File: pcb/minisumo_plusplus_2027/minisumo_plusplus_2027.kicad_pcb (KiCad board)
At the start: 2 copper layers, 45 x 33 mm, 11 parts, among them J1 IR - Conn_01x03_Pin, J2 IR - Conn_01x03_Pin, J3 Start Module - Conn_01x04_Pin, J4 US - Conn_01x04_Pin, SW1 SW_SPDT, U3 ESP32-C6-SuperMini

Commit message: pcb updates to clean up a abit, drc was quite ok!
folders & inspiration images of lego and death racer robots
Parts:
- moved REF** 222.2 mm to (41.8, 107.4)
- moved REF** 222.2 mm to (41.4, 117.3)
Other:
- board size 45 x 33 mm -> 210.2 x 100 mm
- board text added: "3d packaging concept"
- board text added: "GND /IN-"
- board text removed: "GND/IN-"

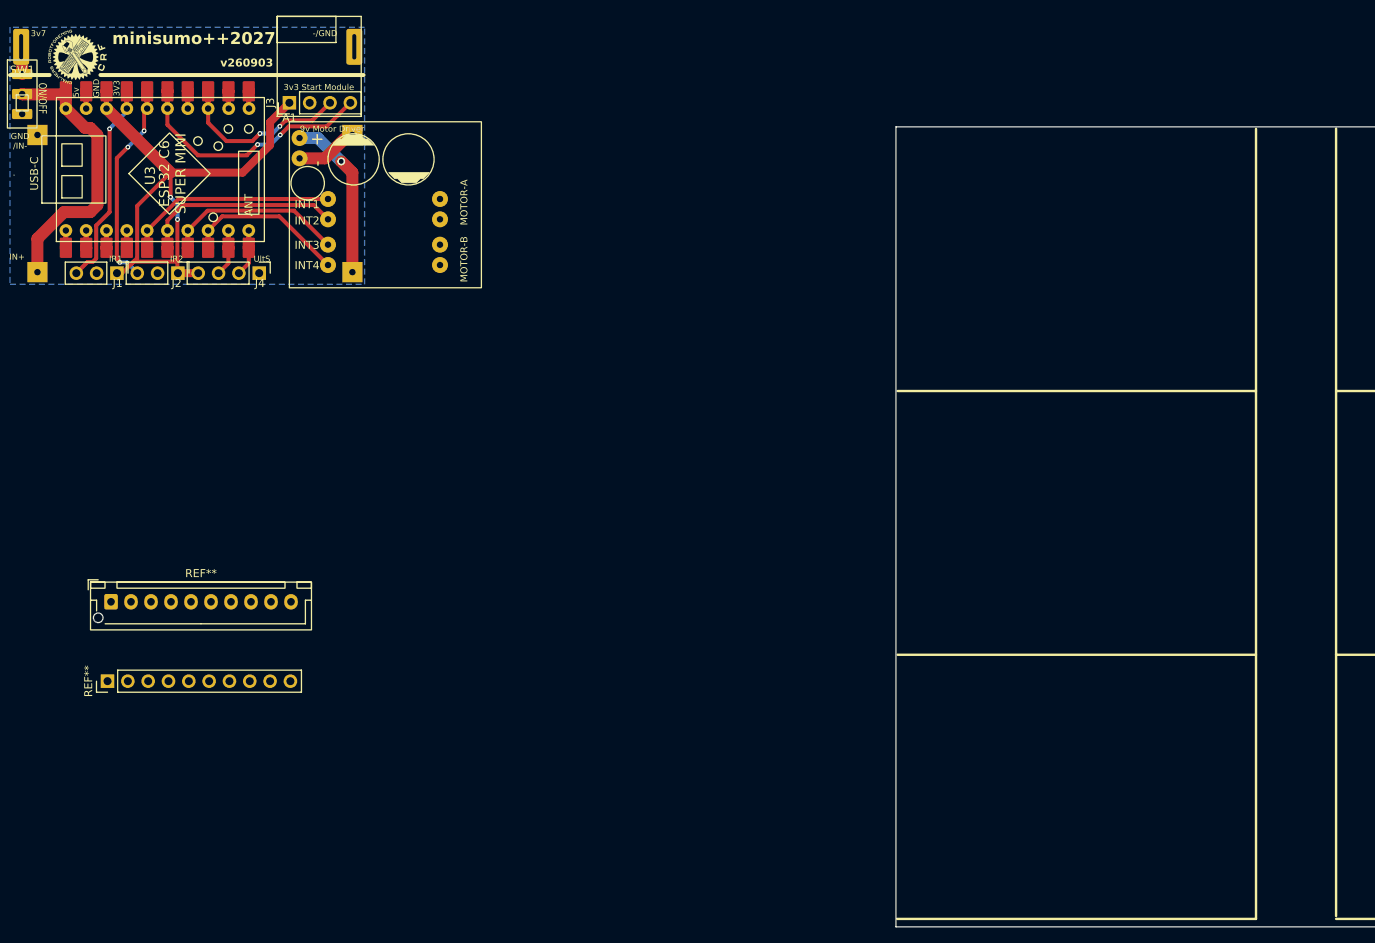
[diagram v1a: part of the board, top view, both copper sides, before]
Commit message: cleaned up pcb more and fixed / prepared for the eventual migration to the 10x10 inkl extra stripboard!
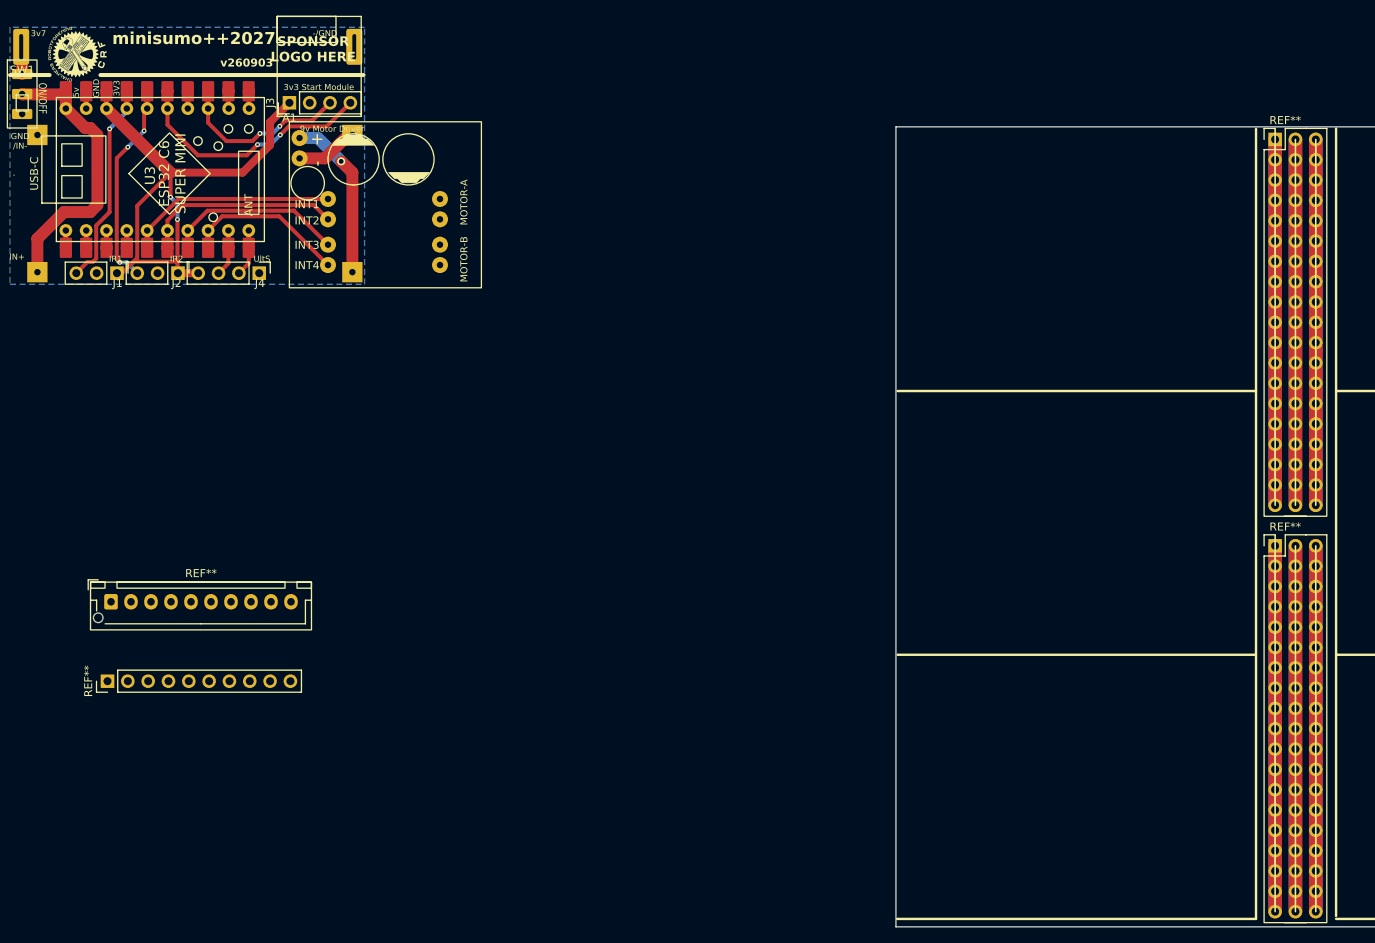
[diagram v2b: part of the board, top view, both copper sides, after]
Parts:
- added REF**: Stripboard_3x19_P2.54mm, minisumo_plusplus_2027:Stripboard_3x19_P2.54mm, F.Cu at (187.4, 49.6)
- added REF**: Stripboard_3x19_P2.54mm, minisumo_plusplus_2027:Stripboard_3x19_P2.54mm, F.Cu at (187.4, 100.4)
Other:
- board text added: "SPONSOR LOGO HERE"

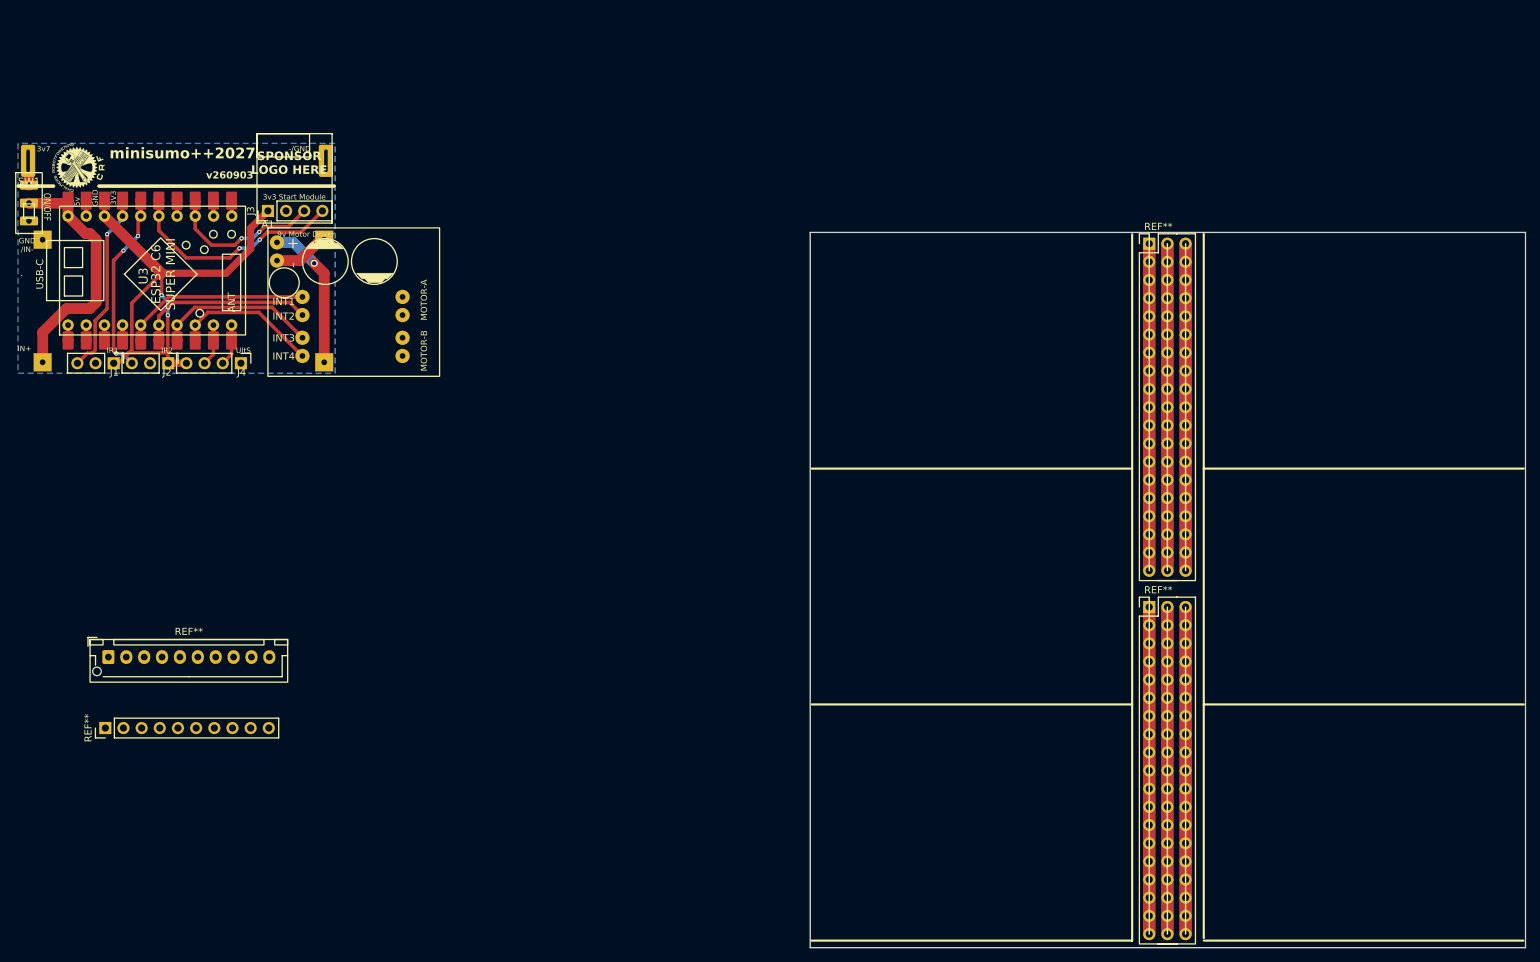
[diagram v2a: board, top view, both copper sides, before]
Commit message: pcb kicad fixed zoom issue! (extranous bits somewhere..)
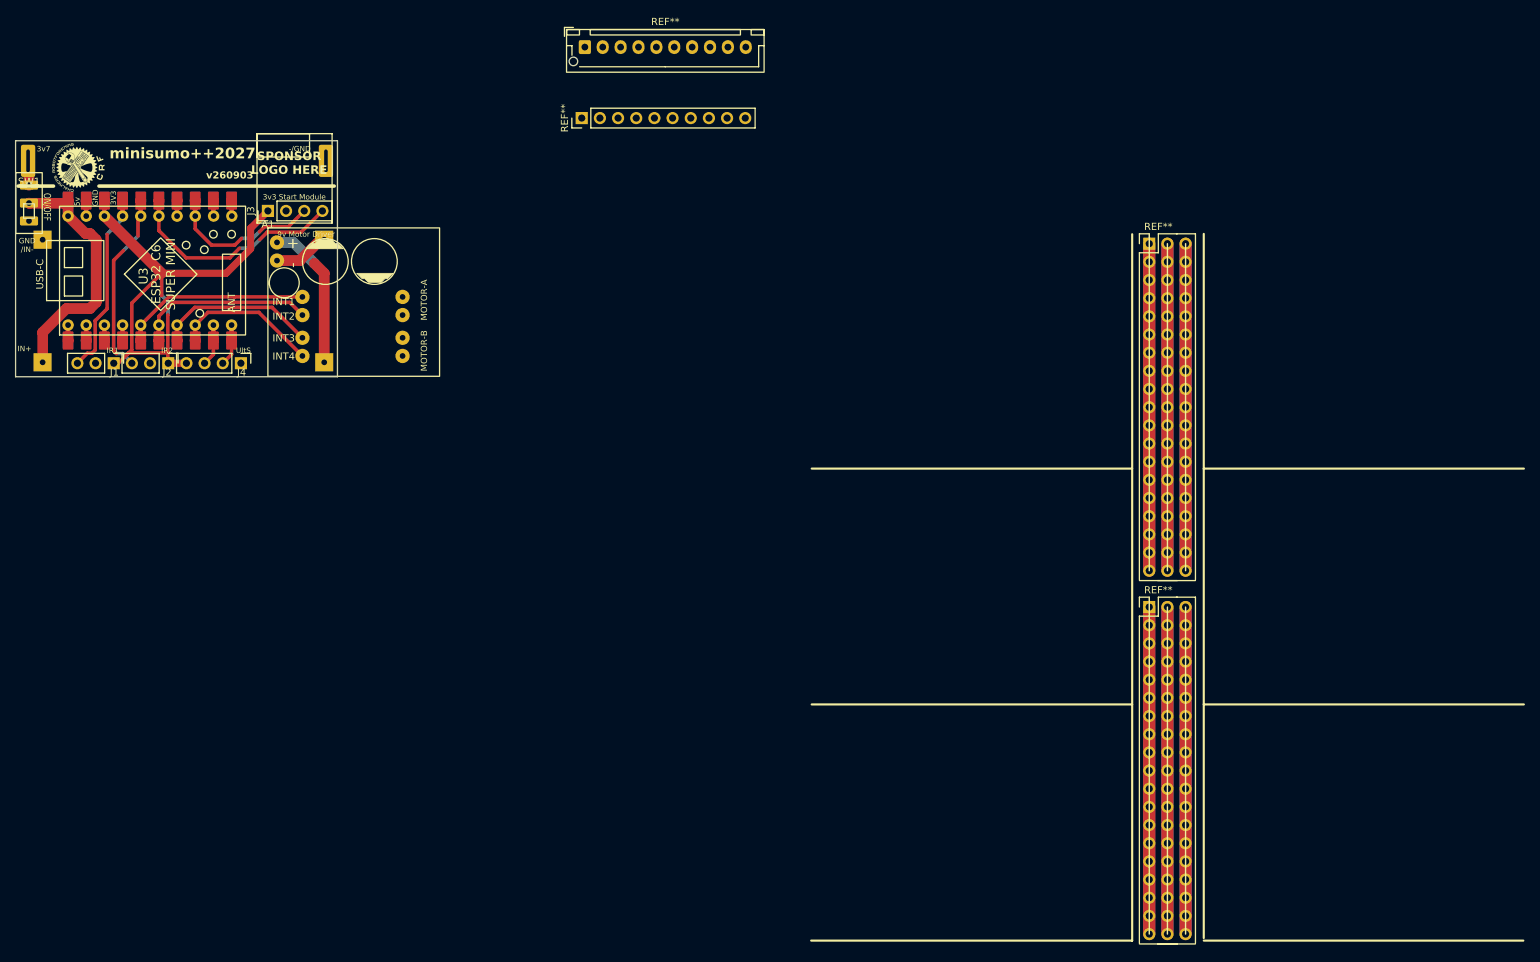
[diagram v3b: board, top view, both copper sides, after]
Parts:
- moved REF** 108.2 mm to (108.4, 22.1)
- moved REF** 108.2 mm to (108.0, 32.0)
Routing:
- net START Start: vias 2 -> 0
- net START Kill - not mandatory for sumo: vias 2 -> 0
- net IR Rear: vias 3 -> 0
- net IR Front: vias 1 -> 0
- net 3v3: vias 2 -> 0
- net /9v: vias 1 -> 0
- removed copper zone on B.Cu, net GND
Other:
- board size 210.2 x 100 mm -> 45 x 33 mm

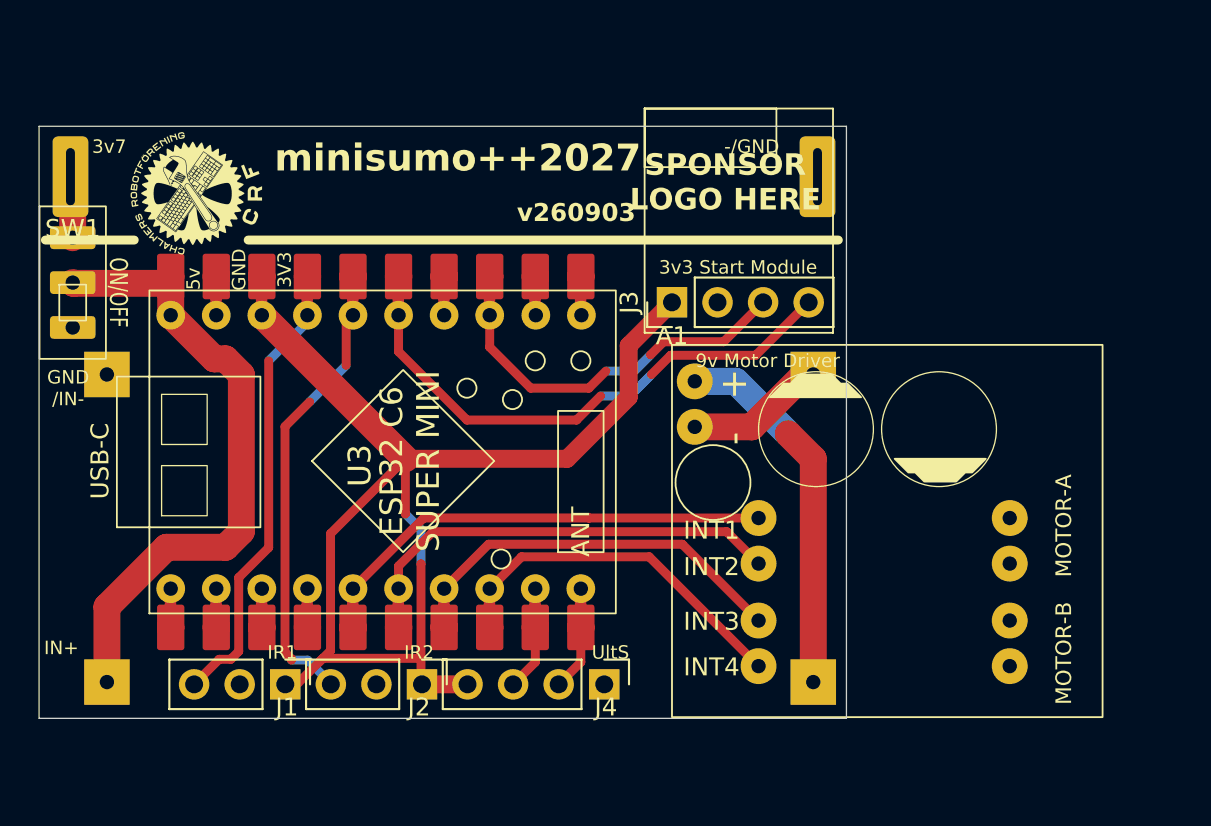
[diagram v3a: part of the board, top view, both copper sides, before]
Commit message: pcb fixing silkscreens and cleanups based primarily on esp32 c6 improved batt pads and middle board pin positions based on images
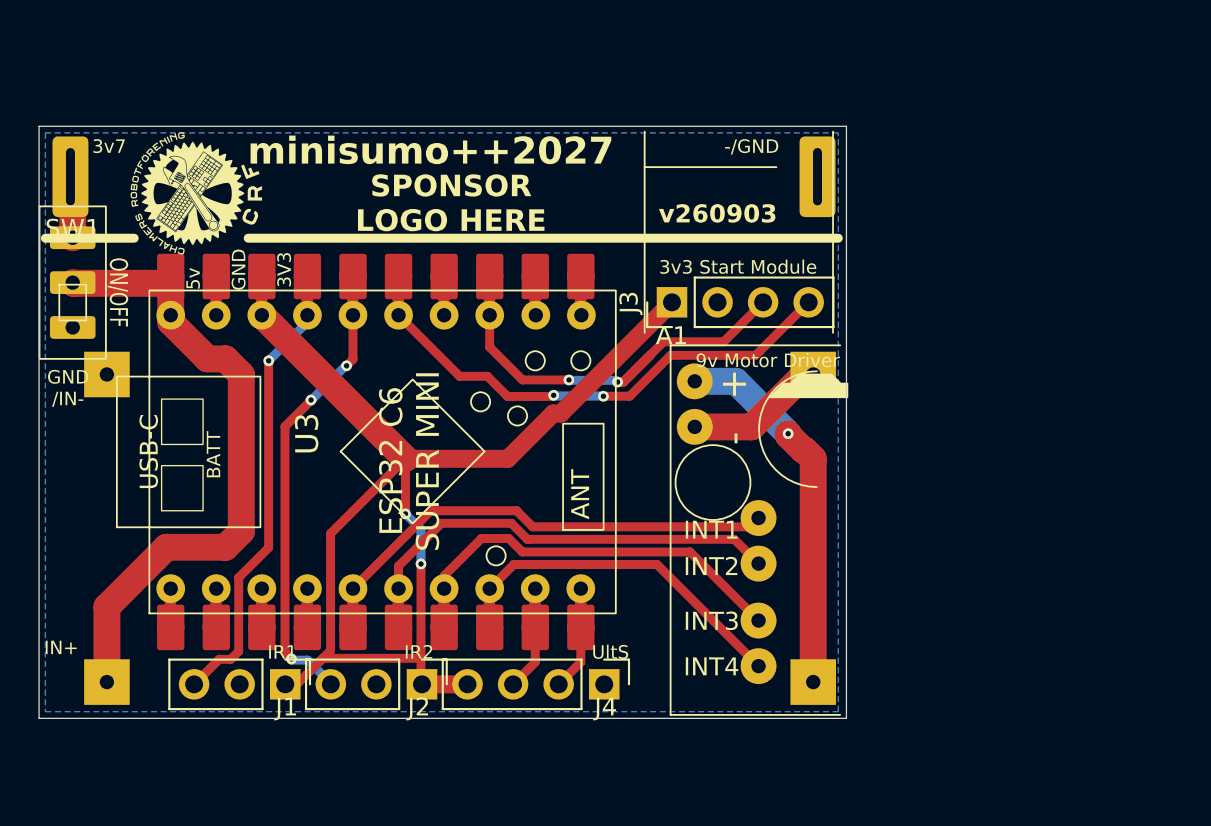
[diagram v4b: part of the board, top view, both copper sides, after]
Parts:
- A1: footprint minisumo_plusplus_2027:Mini_L298N_2_Channel_H_Bridge_DC_Motor_Driver_Board_with_MX1508 -> minisumo_plusplus_2027:Mini_L298N_2_Channel_H_Bridge_DC_Motor_Driver_Board_with_MX1508-special_silk
- U2: footprint BBQ_Library:battery cr123 3.7v with contacts for 18650 -> minisumo_plusplus_2027:battery cr123 3.7v with contacts for 18650_special_silk
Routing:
- net START Start: track 22.1 -> 26.7 mm, vias 0 -> 2
- net IR Rear: track 25.4 -> 28.2 mm, vias 0 -> 3
- net START Kill - not mandatory for sumo: track 31.3 -> 29.1 mm, vias 0 -> 2
- net 3v3: track 68.2 -> 66.5 mm, vias 0 -> 2
- net Net-(A1-INT3): track 22.5 -> 23.2 mm
- net /9v: track 20.8 -> 20.9 mm, vias 0 -> 1
- net IR Front: vias 0 -> 1
- added copper zone on B.Cu, net (none)
